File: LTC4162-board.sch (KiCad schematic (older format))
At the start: 67 parts, among them J2 Conn_01x02, J3 Conn_02x03_Odd_Even, J4 Conn_01x02, Q1 Q_NMOS_GDS, Q2 Q_NMOS_GDS, U1 LTC4162-L

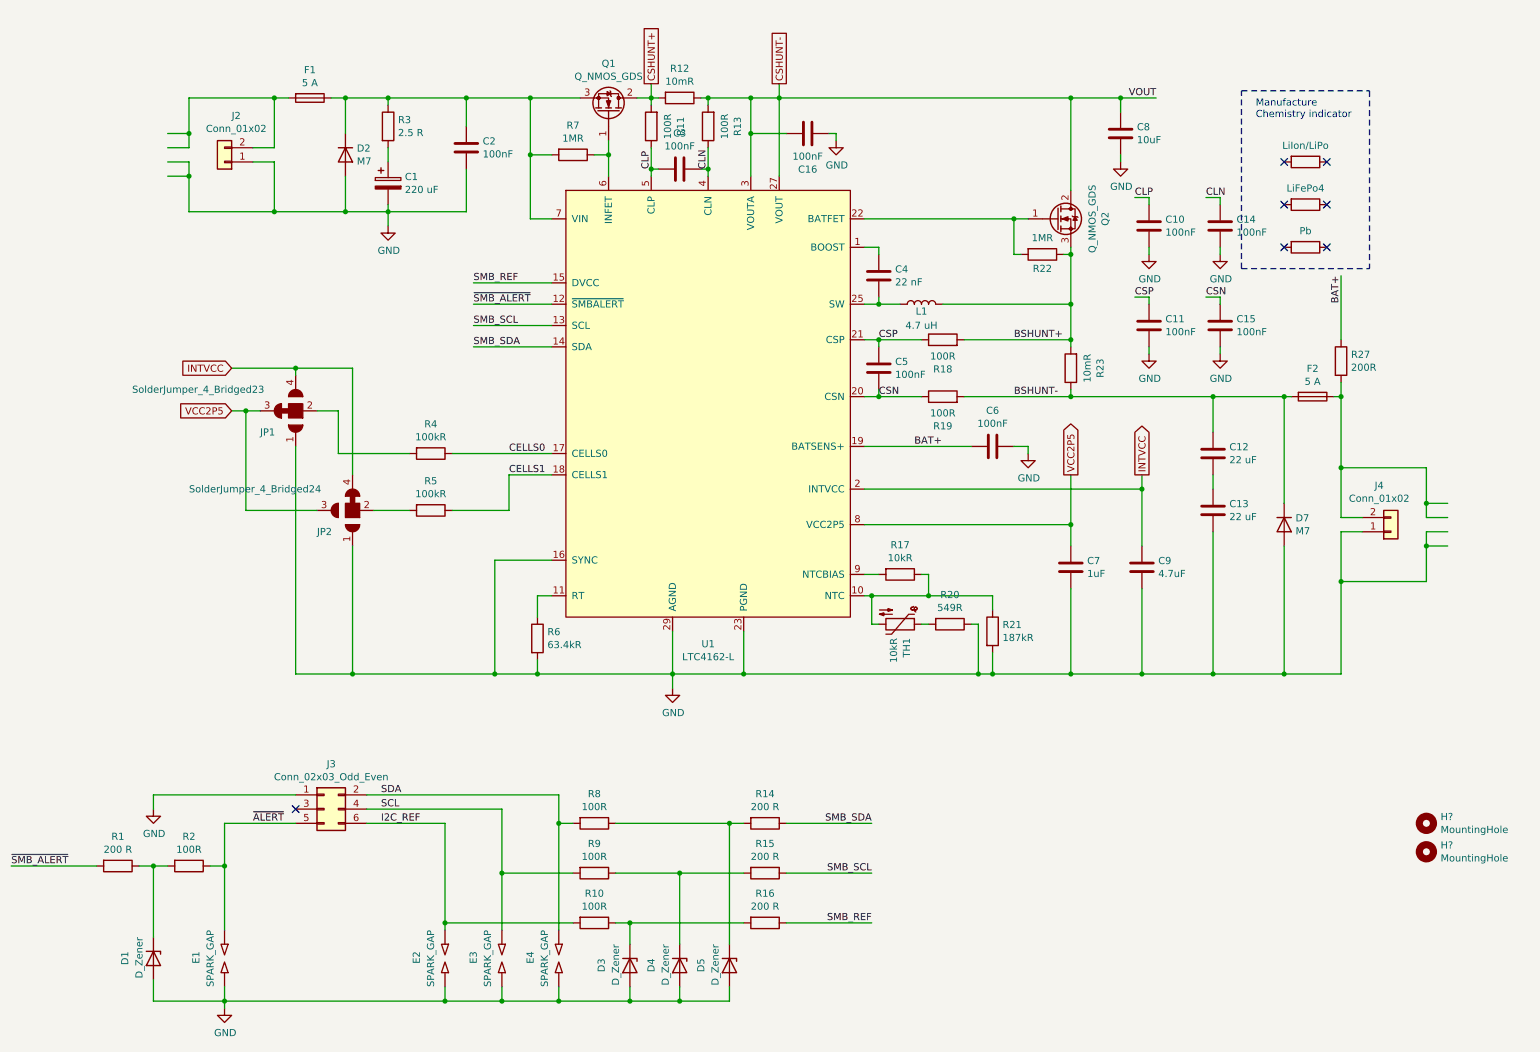
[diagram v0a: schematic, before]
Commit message: Optimize for basic parts
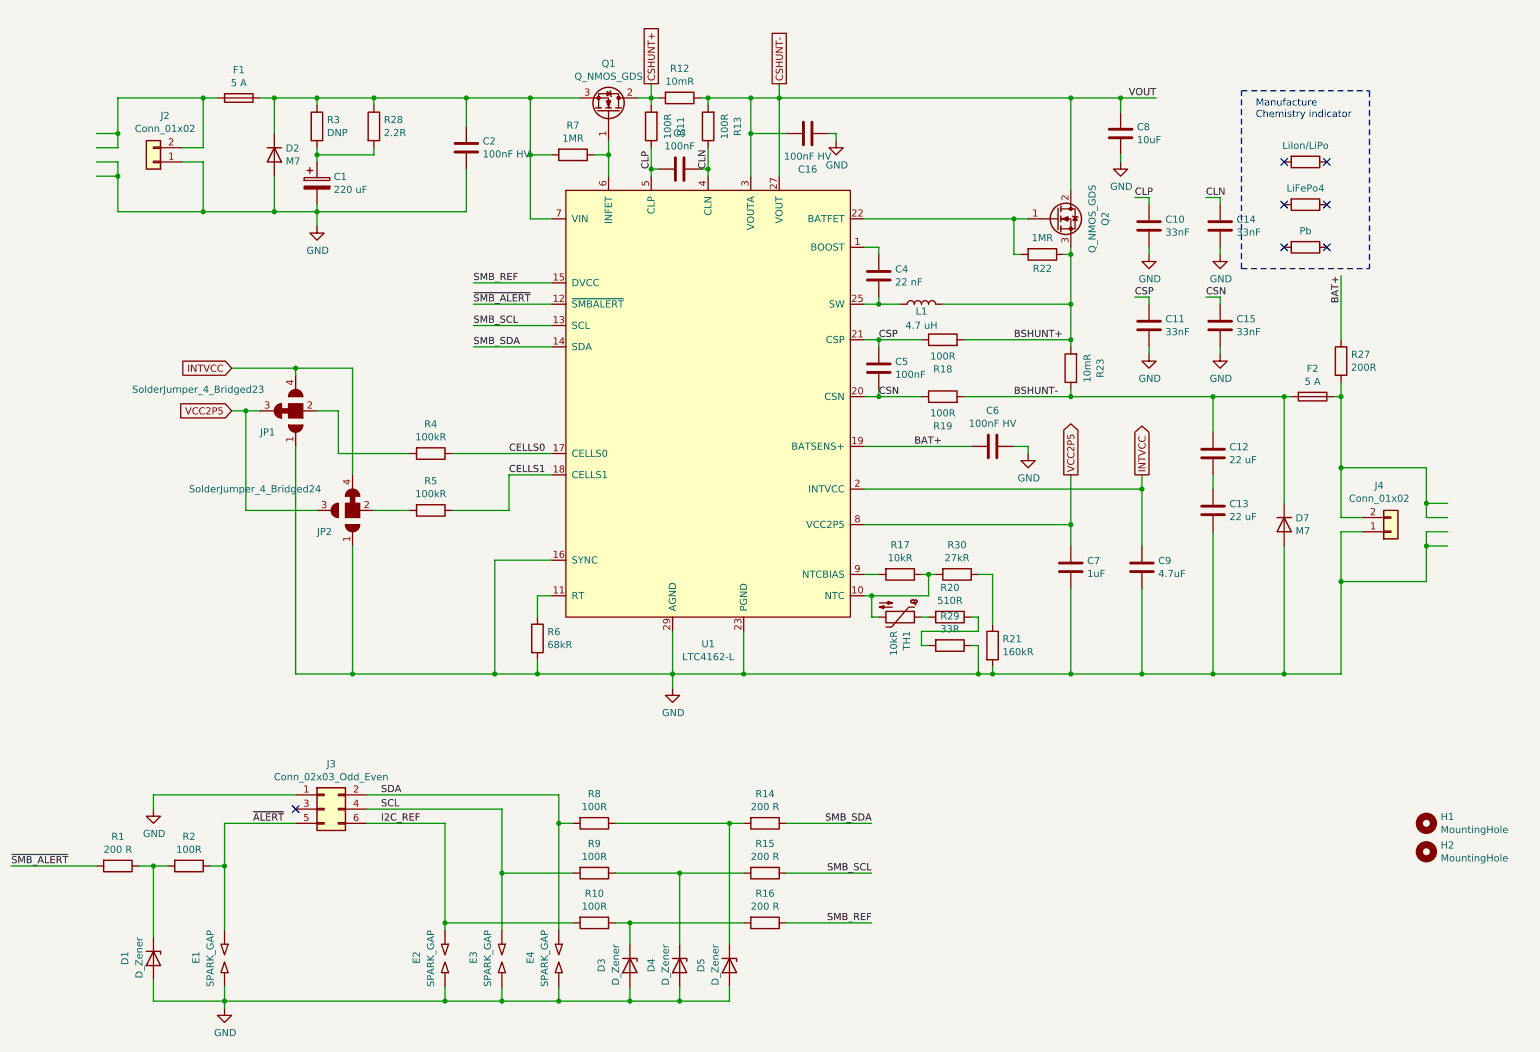
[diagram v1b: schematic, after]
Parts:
- added R28: 2.2R, Resistor_SMD:R_0805_2012Metric, symbol Device:R
- added R29: 33R, Resistor_SMD:R_0402_1005Metric, symbol Device:R
- added R30: 27kR, Resistor_SMD:R_0402_1005Metric, symbol Device:R
- C10, C11, C15: value 100nF -> 33nF; LCSC 1525 -> C1585
- C14: value 100nF -> 33nF; LCSC C1525 -> C1585
- C16, C2, C6: value 100nF -> 100nF HV
- R20: value 549R -> 510R; footprint Resistor_SMD:R_0603_1608Metric -> Resistor_SMD:R_0402_1005Metric; LCSC C23079 -> C25123
- R21: value 187kR -> 160kR; footprint Resistor_SMD:R_0402_1005Metric -> Resistor_SMD:R_0603_1608Metric; LCSC C25761 -> C22813
- R3: value 2.5 R -> DNP; LCSC C247183 -> (none)
- R6: value 63.4kR -> 68kR; LCSC C38606 -> C36871
- gave numbers to parts that had none: 2
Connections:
- wire segments 244 -> 255
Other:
- moved on the sheet: C1, D2, F1, J2, R20, R21, R3, TH1

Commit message: Export schematic as pdf
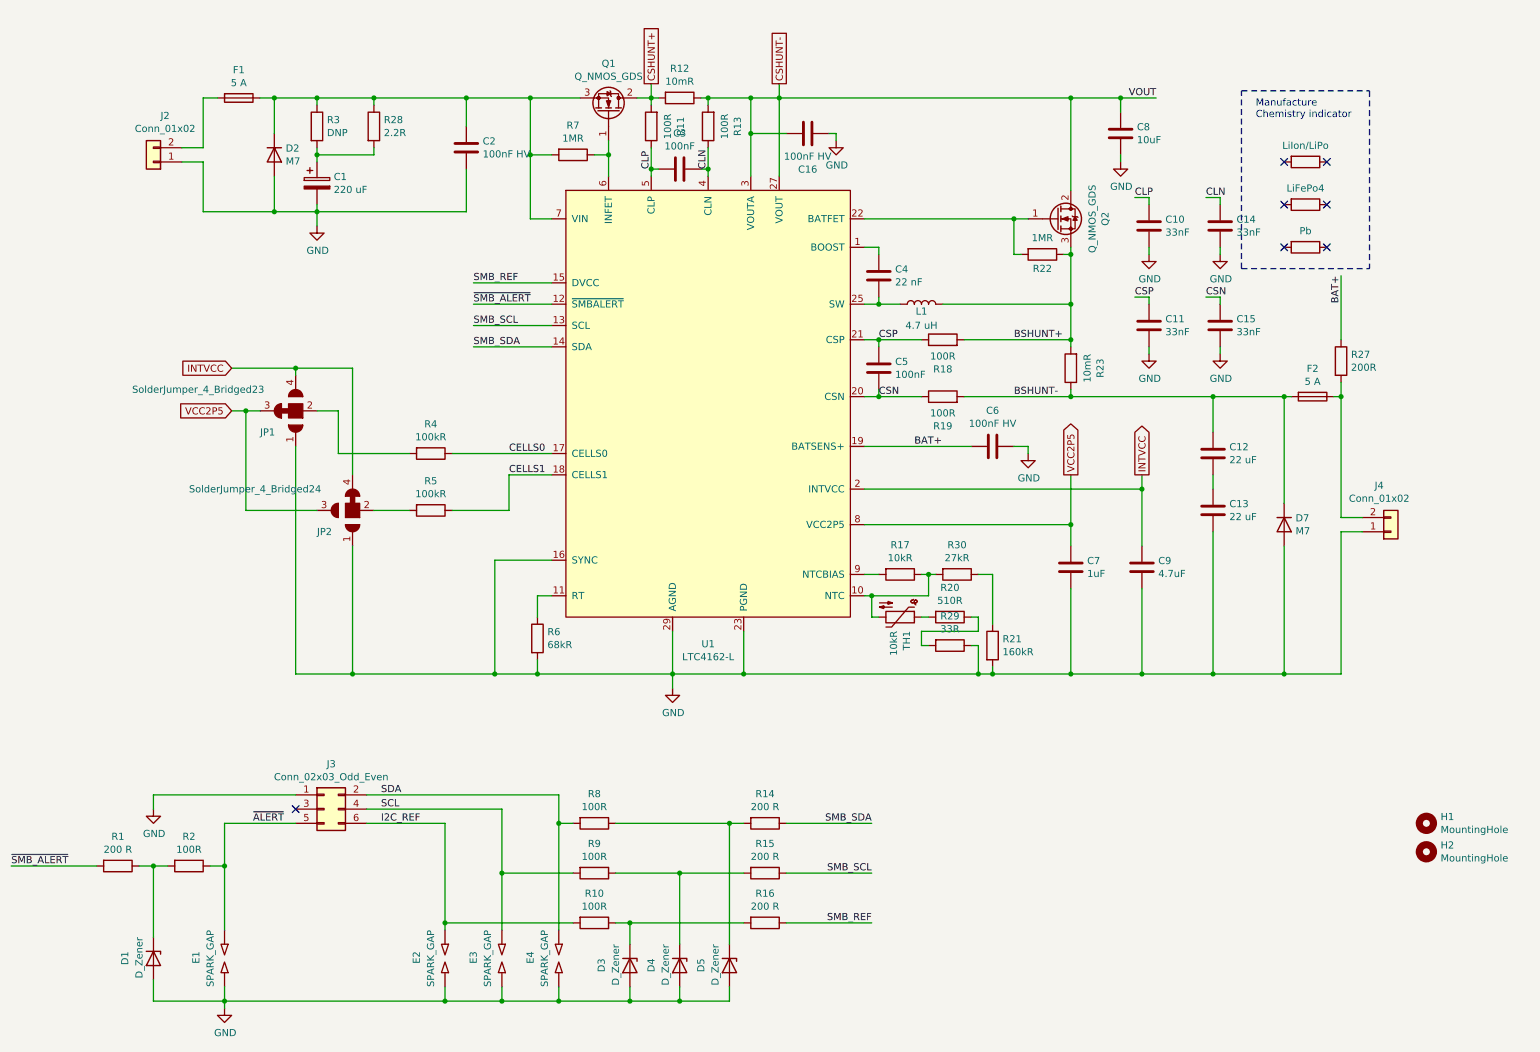
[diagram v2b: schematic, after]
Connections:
- wire segments 255 -> 233
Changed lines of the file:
@@
 Wire Wire Line
 	9050 3450 9050 3200
-Wire Wire Line
-	1200 1450 1350 1450
-Wire Wire Line
-	1350 1450 1350 1350
-Wire Wire Line
-	1350 1350 1200 1350
-Wire Wire Line
-	1200 1550 1350 1550
-Wire Wire Line
-	1350 1550 1350 1650
-Wire Wire Line
-	1350 1650 1200 1650
-Wire Wire Line
-	1350 1100 1350 1350
-Wire Wire Line
-	1350 1100 1950 1100
-Connection ~ 1350 1350
-Connection ~ 1350 1650
 $Comp
 L Connector_Generic:Conn_01x02 J?
@@
 	2750 1900 2750 1850
 Wire Wire Line
-	1350 1900 1350 1650
-Wire Wire Line
 	1950 1550 1950 1900
-Wire Wire Line
-	1950 1900 1350 1900
 Wire Wire Line
 	8050 4100 8050 3750
@@
 Wire Wire Line
 	2050 1100 1950 1100
-Connection ~ 1950 1100
 Wire Wire Line
 	2450 1900 2750 1900
@@
 	2450 1900 1950 1900
 Connection ~ 2450 1900
-Connection ~ 1950 1900
 Text Label 4100 3600 0    50   ~ 0
 CELLS0
@@
 	0    1    1    0
 $EndComp
-Wire Wire Line
-	10700 4150 10550 4150
-Wire Wire Line
-	10550 4150 10550 4250
-Wire Wire Line
-	10550 4250 10700 4250
-Wire Wire Line
-	10700 4050 10550 4050
-Wire Wire Line
-	10550 4050 10550 3950
-Wire Wire Line
-	10550 3950 10700 3950
-Wire Wire Line
-	10550 4500 10550 4250
-Wire Wire Line
-	10550 4500 9950 4500
-Connection ~ 10550 4250
-Connection ~ 10550 3950
 $Comp
 L Connector_Generic:Conn_01x02 J?
@@
 	10100 4150 9950 4150
 Wire Wire Line
-	9950 4150 9950 4500
-Wire Wire Line
 	10100 4050 9950 4050
-Wire Wire Line
-	10550 3700 10550 3950
-Wire Wire Line
-	9950 4050 9950 3700
-Wire Wire Line
-	9950 3700 10550 3700
 Wire Wire Line
 	9900 3200 9950 3200
@@
 	9600 3200 9550 3200
 Connection ~ 9550 3200
-Wire Wire Line
-	9950 3700 9950 3200
-Connection ~ 9950 3700
 Connection ~ 9950 3200
 Wire Wire Line
-	9950 4500 9950 5150
-Wire Wire Line
 	9950 5150 9550 5150
-Connection ~ 9950 4500
 Connection ~ 9550 5150
 $Comp
@@
 	7100 4450 7050 4450
 Connection ~ 7050 4450
+Wire Wire Line
+	9950 4150 9950 5150
+Wire Wire Line
+	9950 3200 9950 4050
 $EndSCHEMATC
